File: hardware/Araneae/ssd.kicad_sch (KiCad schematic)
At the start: 8 parts, among them J1 MDT320M01001, Y1 32.768kHz

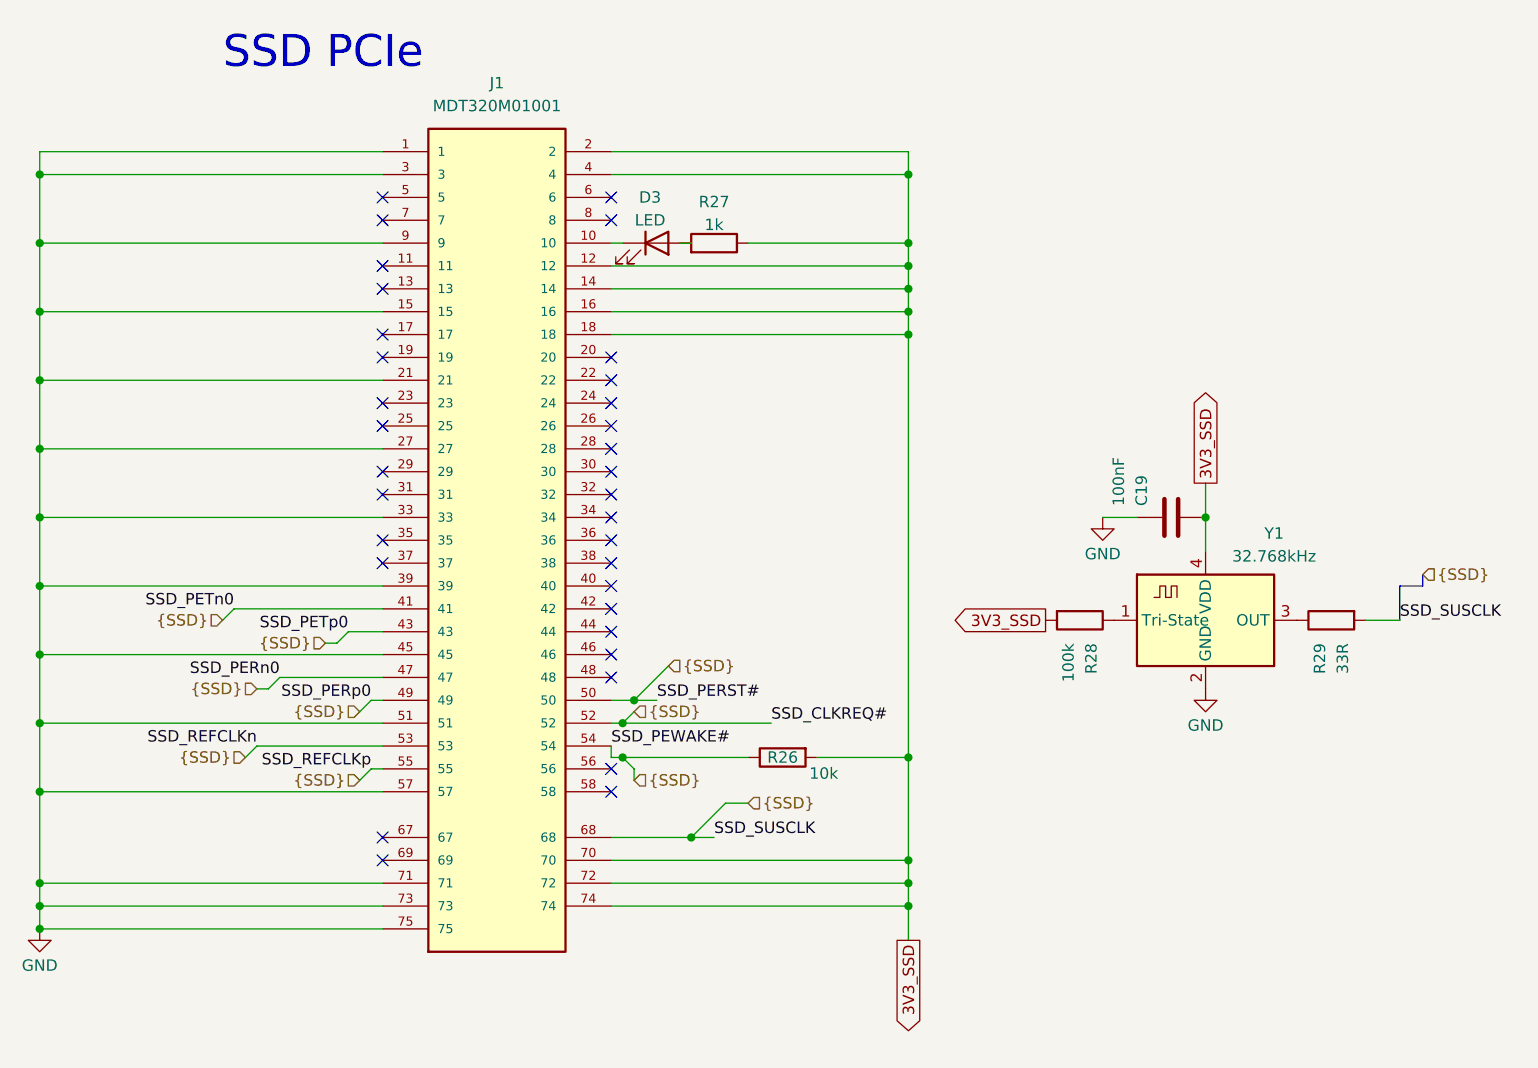
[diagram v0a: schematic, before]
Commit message: Add CI workflow for PCB checks and artifact generation
- Created a GitHub Actions workflow (`ci.yml`) to automate hardware checks including ERC, DRC, and plot generation for KiCad projects.
- Added a new footprint for the SON50P200X200X80-9N component in `SON50P200X200X80-9N.kicad_mod`.
- Introduced a new symbol for the TPS22965DSGR component in `TPS22965DSGR.kicad_sym`.
- Added a configuration file `kibot.yaml` for generating fabrication files and other outputs.
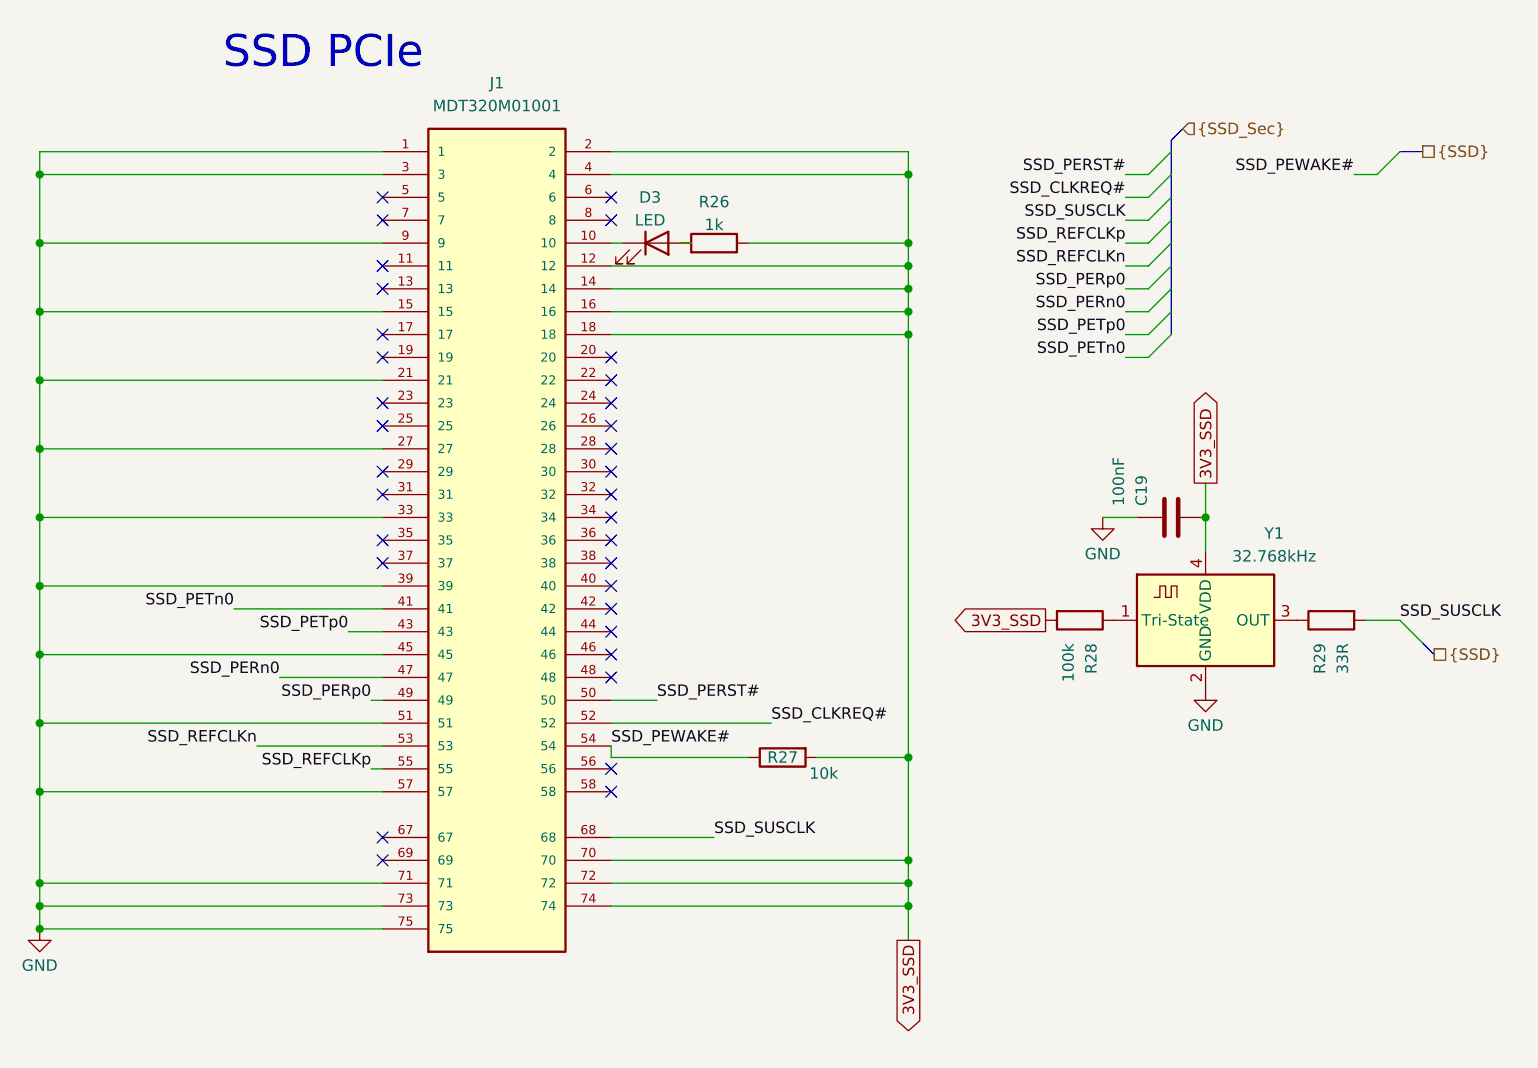
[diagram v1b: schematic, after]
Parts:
- C19: footprint (none) -> Capacitor_SMD:C_0603_1608Metric
- D3: footprint (none) -> LED_SMD:LED_0805_2012Metric
- J1: footprint MDT320M01001:AMPHENOL_MDT320M01001 -> OPL:AMPHENOL_MDT320M01001
- R26: renamed from R27; footprint (none) -> Resistor_SMD:R_0603_1608Metric
- R27: renamed from R26; footprint (none) -> Resistor_SMD:R_0603_1608Metric
- R28, R29: footprint (none) -> Resistor_SMD:R_0603_1608Metric
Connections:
- net {SSD}: no longer J1.41, J1.43, J1.47, J1.49, J1.50, J1.52, J1.53, J1.54, J1.55, J1.68, R27.1, R29.2
- new net SSD_CLKREQ#: J1.52
- new net SSD_PERST#: J1.50
- new net SSD_PERn0: J1.47
- new net SSD_PERp0: J1.49
- new net SSD_PETn0: J1.41
- new net SSD_PETp0: J1.43
- new net SSD_PEWAKE#: J1.54, R27.1
- new net SSD_REFCLKn: J1.53
- new net SSD_REFCLKp: J1.55
- new net SSD_SUSCLK: J1.68, R29.2
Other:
- company: (none) -> Matheus Henrique(Aka: TheusHen)
- title: (none) -> Araneae
